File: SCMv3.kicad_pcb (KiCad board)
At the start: 2 copper layers, 58.7 x 110.9 mm, 122 parts, among them IC1 40106, IC2 40106, IC3 TL082, J1 ISP, J1-OUT8 JACK-MONO-SWB, J2 Conn_01x02, J2-OUT7 JACK-MONO-SWB, J3 POWER, J3-OUT6 JACK-MONO-SWB, J4-OUT5 JACK-MONO-SWB, J5-OUT4 JACK-MONO-SWB, J6-OUT3 JACK-MONO-SWB, J7-OUT2 JACK-MONO-SWB, J8-OUT1 JACK-MONO-SWB, J9-CLK_IN1 JCLK_IN, Q1 Si2318, Q2 Si2318, Q3 Si2318, Q4 Si2318, U1 ATmega328-A, Y1 16MHz_18pF_FA238

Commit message: Moved XTAL caps (C4, C5) GND trace to go directly to uc (U1)
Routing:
- net GND: track 698.8 -> 691.5 mm, vias 56 -> 54
- net +5V: track 225.1 -> 224.6 mm
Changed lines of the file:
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@@
     (effects (font (size 0.9652 0.9652) (thickness 0.12192)) (justify left bottom mirror))
   )
-  (segment (start 19.55 77.67) (end 19.55 79.45) (width 0.2032) (layer "F.Cu") (net 1))
   (segment (start 19.38 69.08) (end 19.68 68.78) (width 0.25) (layer "F.Cu") (net 1))
   (segment (start 6.98 85.52) (end 9.3 83.2) (width 0.25) (layer "F.Cu") (net 1))
@@
   (segment (start 31.82 104.3325) (end 31.14 103.6525) (width 0.2032) (layer "F.Cu") (net 1))
   (segment (start 31.09 79.3282) (end 30.9282 79.49) (width 0.2032) (layer "F.Cu") (net 1))
+  (segment (start 16.908889 73.061111) (end 17.94 72.03) (width 0.2032) (layer "F.Cu") (net 1))
   (segment (start 6.280902 85.52) (end 6.98 85.52) (width 0.25) (layer "F.Cu") (net 1))
   (segment (start 19.59 71.904022) (end 19.59 70.98) (width 0.25) (layer "F.Cu") (net 1))
@@
   (segment (start 34.03 52.99) (end 37.01 55.97) (width 0.2032) (layer "F.Cu") (net 1))
   (segment (start 13.67 88.43076) (end 11.11076 88.43076) (width 0.25) (layer "F.Cu") (net 1))
-  (segment (start 19.55 79.45) (end 20.04 79.94) (width 0.2032) (layer "F.Cu") (net 1))
   (segment (start 21.19 79.02) (end 21.19 80.57) (width 0.25) (layer "F.Cu") (net 1))
   (segment (start 55.84 62.1) (end 57.0738 63.3338) (width 0.2032) (layer "F.Cu") (net 1))
@@
   (segment (start 8.67 33.42) (end 8.67 31.69) (width 0.2032) (layer "F.Cu") (net 1))
   (segment (start 34.03 52.18) (end 34.03 52.99) (width 0.2032) (layer "F.Cu") (net 1))
+  (segment (start 16.908889 74.588889) (end 16.908889 73.061111) (width 0.2032) (layer "F.Cu") (net 1))
   (segment (start 4.83 86.57076) (end 5.230142 86.57076) (width 0.25) (layer "F.Cu") (net 1))
+  (segment (start 17.94 72.03) (end 17.99 72.03) (width 0.2032) (layer "F.Cu") (net 1))
   (segment (start 22.1 94.67) (end 22.1 95.90924) (width 0.2032) (layer "F.Cu") (net 1))
   (segment (start 14.330143 79.639857) (end 15.07 78.9) (width 0.25) (layer "F.Cu") (net 1))
@@
   (segment (start 13.823801 15.056199) (end 13.95 14.93) (width 0.25) (layer "F.Cu") (net 1))
   (segment (start 21.13 47.33) (end 18.87 47.33) (width 0.25) (layer "F.Cu") (net 1))
+  (segment (start 17.71 75.39) (end 16.908889 74.588889) (width 0.2032) (layer "F.Cu") (net 1))
   (segment (start 21.19 80.57) (end 21.95 81.33) (width 0.25) (layer "F.Cu") (net 1))
   (segment (start 33.8632 51.31) (end 31.82 51.31) (width 0.2032) (layer "F.Cu") (net 1))
@@
   (via (at 27.14 62.78) (size 0.8) (drill 0.4) (layers "F.Cu" "B.Cu") (net 1))
   (via (at 31.38 50.87) (size 0.8) (drill 0.4) (layers "F.Cu" "B.Cu") (net 1))
-  (via (at 20.04 79.94) (size 0.8) (drill 0.4) (layers "F.Cu" "B.Cu") (net 1))
   (via (at 27.14 62.78) (size 0.8) (drill 0.4) (layers "F.Cu" "B.Cu") (net 1))
   (via (at 21.95 81.33) (size 0.8) (drill 0.4) (layers "F.Cu" "B.Cu") (net 1))
   (via (at 13.099299 72.56) (size 0.8) (drill 0.4) (layers "F.Cu" "B.Cu") (net 1))
-  (via (at 20.04 79.94) (size 0.8) (drill 0.4) (layers "F.Cu" "B.Cu") (net 1))
   (via (at 24.39 17.6) (size 0.8) (drill 0.4) (layers "F.Cu" "B.Cu") (net 1))
   (via (at 37.01 55.97) (size 0.8) (drill 0.4) (layers "F.Cu" "B.Cu") (net 1))
@@
   (via (at 55.84 62.1) (size 0.8) (drill 0.4) (layers "F.Cu" "B.Cu") (net 1))
   (via (at 19.68 68.78) (size 0.8) (drill 0.4) (layers "F.Cu" "B.Cu") (net 1))
-  (segment (start 18.81 81.17) (end 13.722306 81.17) (width 0.2032) (layer "B.Cu") (net 1))
   (segment (start 22.6403 9.0297) (end 25.527 9.0297) (width 0.2032) (layer "B.Cu") (net 1))
   (segment (start 10.337963 72.629457) (end 13.029844 72.629457) (width 0.2032) (layer "B.Cu") (net 1))
@@
   (segment (start 27.14 67.5) (end 25.527 69.113) (width 0.2032) (layer "B.Cu") (net 1))
   (segment (start 6.623857 44.333857) (end 12.192163 44.333857) (width 0.25) (layer "B.Cu") (net 1))
-  (segment (start 13.722306 81.17) (end 12.192163 79.639857) (width 0.2032) (layer "B.Cu") (net 1))
   (segment (start 5.24 88.43) (end 4.75 87.94) (width 0.25) (layer "B.Cu") (net 1))
   (segment (start 22.57 9.1) (end 22.6403 9.0297) (width 0.2032) (layer "B.Cu") (net 1))
@@
   (segment (start 27.94 85.2297) (end 25.527 85.2297) (width 0.25) (layer "B.Cu") (net 1))
   (segment (start 19.12 27.07) (end 18.03 25.98) (width 0.2032) (layer "B.Cu") (net 1))
-  (segment (start 20.04 79.94) (end 18.81 81.17) (width 0.2032) (layer "B.Cu") (net 1))
   (segment (start 26.59 104.64) (end 25.91 105.32) (width 0.2032) (layer "B.Cu") (net 1))
   (segment (start 25.527 26.673) (end 25.527 21.7297) (width 0.2032) (layer "B.Cu") (net 1))
@@
   (segment (start 6.159663 38.225157) (end 6.159663 42.623765) (width 0.2032) (layer "F.Cu") (net 2))
   (segment (start 8.82 46.85) (end 8.84 46.87) (width 0.2032) (layer "F.Cu") (net 2))
-  (segment (start 21.1 59.26) (end 21.1 59.81) (width 0.2032) (layer "F.Cu") (net 2))
   (segment (start 7.38924 86.57076) (end 8.6 85.36) (width 0.2032) (layer "F.Cu") (net 2))
   (segment (start 5.257963 54.976457) (end 5.257963 60.371973) (width 0.2032) (layer "F.Cu") (net 2))
@@
   (segment (start 28.725899 54.155899) (end 24.42 49.85) (width 0.2032) (layer "B.Cu") (net 43))
   (segment (start 21.76 16.05) (end 21.73 16.08) (width 0.2032) (layer "F.Cu") (net 44))
+  (segment (start 34.165 4.995) (end 32.447289 6.712711) (width 0.2032) (layer "F.Cu") (net 44))
   (segment (start 21.73 16.08) (end 21.73 20.33) (width 0.2032) (layer "F.Cu") (net 44))
+  (segment (start 35.51 4.995) (end 34.165 4.995) (width 0.2032) (layer "F.Cu") (net 44))
   (segment (start 21.73 22.24898) (end 20.03898 23.94) (width 0.2032) (layer "F.Cu") (net 44))
-  (segment (start 34.807778 4.995) (end 28.89 10.912778) (width 0.2032) (layer "F.Cu") (net 44))
-  (segment (start 28.89 10.912778) (end 28.89 12.42) (width 0.2032) (layer "F.Cu") (net 44))
+  (segment (start 32.447289 8.862711) (end 28.89 12.42) (width 0.2032) (layer "F.Cu") (net 44))
   (segment (start 21.73 20.33) (end 21.73 22.24898) (width 0.2032) (layer "F.Cu") (net 44))
-  (segment (start 35.51 4.995) (end 34.807778 4.995) (width 0.2032) (layer "F.Cu") (net 44))
+  (segment (start 32.447289 6.712711) (end 32.447289 8.862711) (width 0.2032) (layer "F.Cu") (net 44))
   (via (at 21.76 16.05) (size 0.8) (drill 0.4) (layers "F.Cu" "B.Cu") (net 44))
   (via (at 21.76 16.05) (size 0.8) (drill 0.4) (layers "F.Cu" "B.Cu") (net 44))
@@
   (segment (start 40.461289 82.234111) (end 40.461289 92.914389) (width 0.2032) (layer "B.Cu") (net 62))
   (segment (start 41.3124 7.088) (end 40.461289 7.939111) (width 0.2032) (layer "B.Cu") (net 62))
-  (segment (start 35.28611 5.86889) (end 34.583889 5.86889) (width 0.2032) (layer "F.Cu") (net 63))
-  (segment (start 34.583889 10.306111) (end 32.75 12.14) (width 0.2032) (layer "F.Cu") (net 63))
-  (segment (start 34.583889 5.86889) (end 34.583889 10.306111) (width 0.2032) (layer "F.Cu") (net 63))
-  (segment (start 35.51 5.645) (end 35.28611 5.86889) (width 0.2032) (layer "F.Cu") (net 63))
+  (segment (start 35.51 5.645) (end 34.565 5.645) (width 0.2032) (layer "F.Cu") (net 63))
+  (segment (start 34.12 10.77) (end 32.75 12.14) (width 0.2032) (layer "F.Cu") (net 63))
+  (segment (start 34.12 6.09) (end 34.12 10.77) (width 0.2032) (layer "F.Cu") (net 63))
+  (segment (start 34.565 5.645) (end 34.12 6.09) (width 0.2032) (layer "F.Cu") (net 63))
   (segment (start 27.24 2.74) (end 27.56 2.42) (width 0.2032) (layer "F.Cu") (net 64))
   (segment (start 27.56 4.58) (end 27.24 4.9) (width 0.25) (layer "F.Cu") (net 64))
@@
   (segment (start 27.24 4.9) (end 27.24 2.74) (width 0.2032) (layer "F.Cu") (net 64))
   (segment (start 29.61 4.995) (end 27.335 4.995) (width 0.2032) (layer "F.Cu") (net 64))
-  (segment (start 33.36548 5.645) (end 37.62048 1.39) (width 0.2032) (layer "F.Cu") (net 65))
-  (segment (start 37.62048 1.39) (end 50.4628 1.39) (width 0.2032) (layer "F.Cu") (net 65))
-  (segment (start 50.4628 1.39) (end 54.6608 5.588) (width 0.2032) (layer "F.Cu") (net 65))
-  (segment (start 29.61 5.645) (end 33.36548 5.645) (width 0.2032) (layer "F.Cu") (net 65))
+  (segment (start 29.61 5.645) (end 31.934852 5.645) (width 0.2032) (layer "F.Cu") (net 65))
+  (segment (start 50.1328 1.06) (end 54.6608 5.588) (width 0.2032) (layer "F.Cu") (net 65))
+  (segment (start 36.519852 1.06) (end 50.1328 1.06) (width 0.2032) (layer "F.Cu") (net 65))
+  (segment (start 31.934852 5.645) (end 36.519852 1.06) (width 0.2032) (layer "F.Cu") (net 65))
   (segment (start 29.61 5.645) (end 29.61 6.295) (width 0.2032) (layer "F.Cu") (net 65))
   (segment (start 24.83 2.23) (end 25.02 2.42) (width 0.2032) (layer "F.Cu") (net 66))

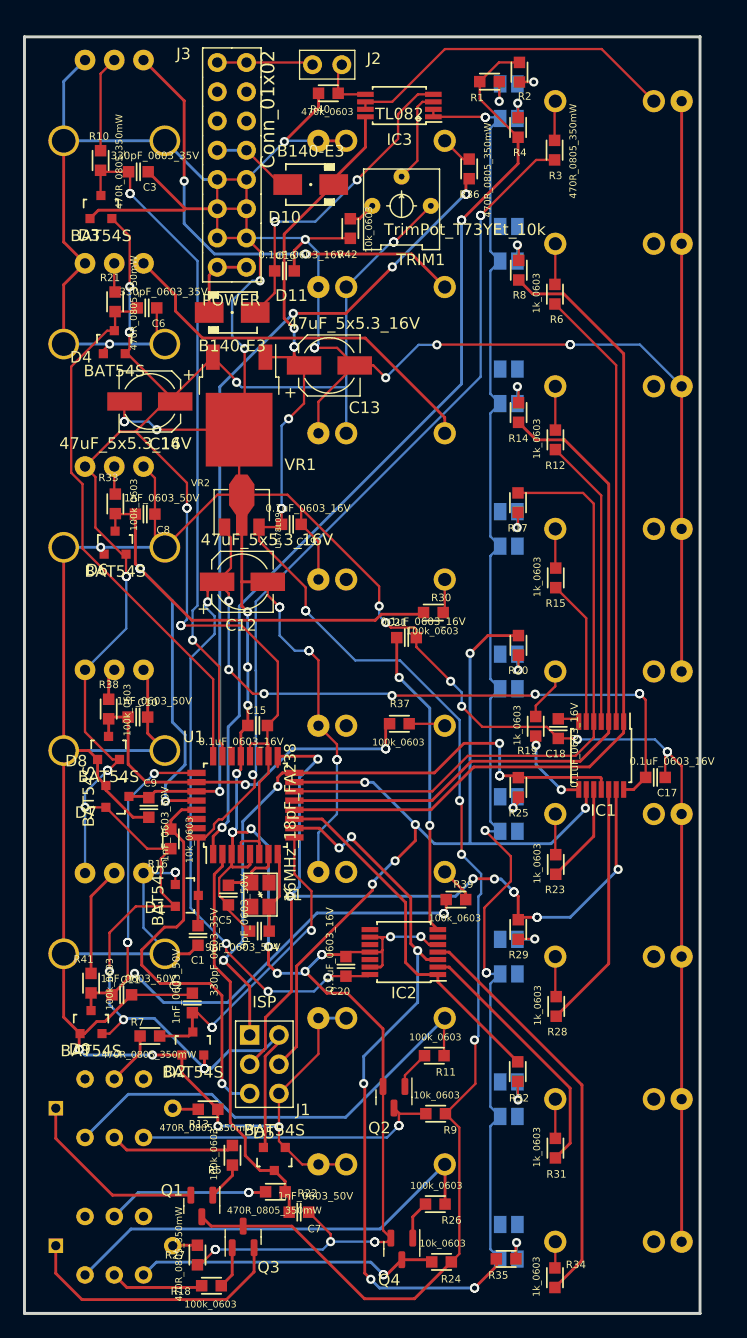
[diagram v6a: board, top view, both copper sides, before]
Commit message: Removed all duplicate Vias. Project ignores silk overlap DRC errors
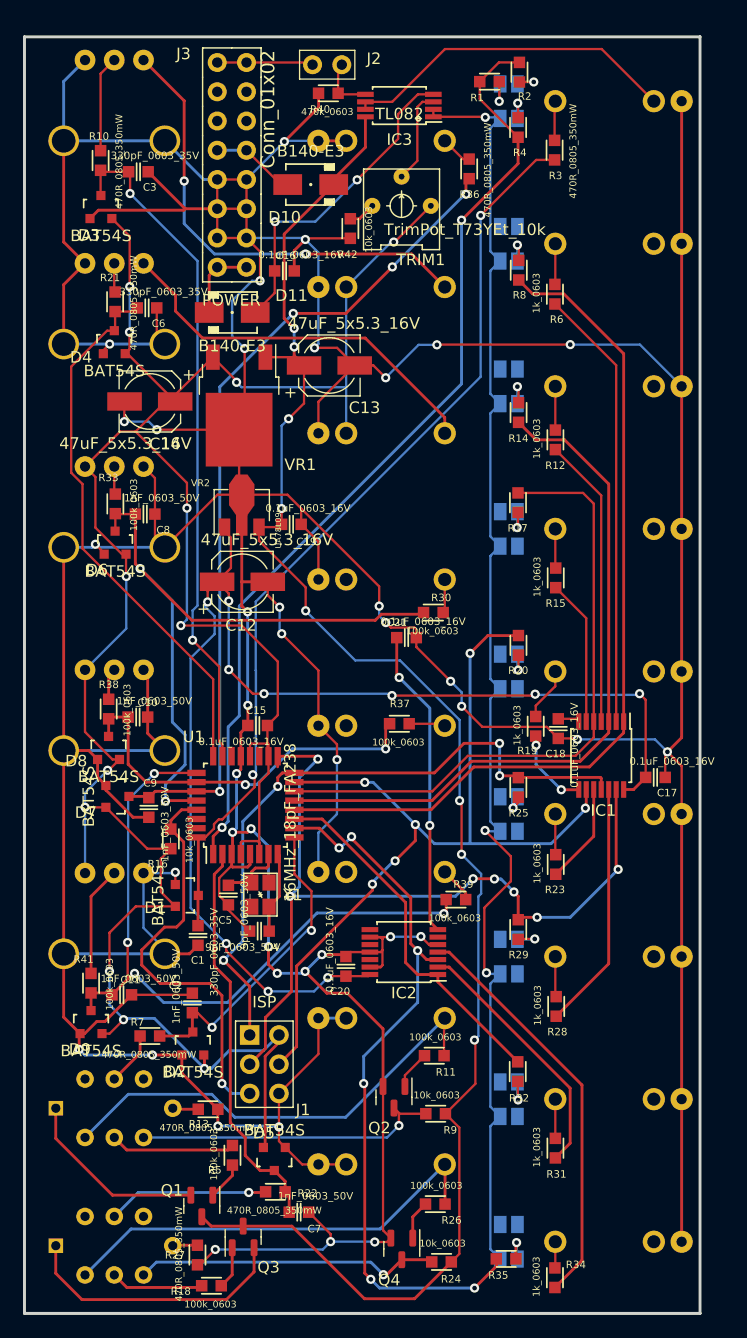
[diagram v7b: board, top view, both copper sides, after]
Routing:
- net GND: track 691.5 -> 699.0 mm, vias 54 -> 40
- net Net-(BMUTE1-Pad6): vias 2 -> 1
- net Net-(BMUTE1-Pad2): vias 2 -> 1
- net Net-(BFAST1-Pad6): vias 2 -> 1
- net /VREF: vias 5 -> 3
- net /UC_SYNC: vias 5 -> 4
- net /UC_SKIP: vias 3 -> 2
- net /UC_SHUFFLE: vias 3 -> 2
- net /UC_ROTATE: vias 3 -> 2
- net /UC_PW: vias 7 -> 4
- net /UC_OUT8: vias 7 -> 6
- net /UC_OUT6_SCK: vias 9 -> 7
- net /UC_OUT5_MISO: vias 5 -> 4
- net /UC_LED_IN: vias 3 -> 2
- net /UC_FAST: vias 3 -> 2
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
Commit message: SILK
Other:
- board text added: "-12V"
- board text added: "ISP"
- board text added: "POWER"
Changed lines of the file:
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@@
     (property "Specifications" "Vreg 5.0V, Iout>500mA, Vin>7V")
     (attr smd)
-    (fp_text reference "VR1" (at 5.14 -5.31 180) (layer "F.SilkS")
+    (fp_text reference "VR1" (at 5.06 -4.95 180) (layer "F.SilkS")
       (effects (font (size 1 1) (thickness 0.15)))
     )
@@
       (effects (font (size 1 1) (thickness 0.15)) (justify left bottom))
     )
-    (fp_text value "POWER" (at -0.05 11.75) (layer "F.SilkS")
+    (fp_text value "POWER" (at -3.28 5.09 90) (layer "F.SilkS")
       (effects (font (size 1 1) (thickness 0.15)))
     )
@@
     (property "Specifications" "470R, 1%, 1/10W, 0603")
     (attr smd)
-    (fp_text reference "R21" (at -2.09 0.44 180) (layer "F.SilkS")
+    (fp_text reference "R21" (at -0.78 1.75 180) (layer "F.SilkS")
       (effects (font (size 0.65 0.65) (thickness 0.15)))
     )
@@
     (property "Specifications" "Dual schottky diode BAT54S")
     (attr smd)
-    (fp_text reference "D4" (at -2.89 1.31) (layer "F.SilkS")
+    (fp_text reference "D4" (at -0.77 2.36) (layer "F.SilkS")
       (effects (font (size 1 1) (thickness 0.15)))
     )
@@
     (property "Specifications" "MOSFET N-chan, 40Vds, Vgs_th=1.2V, Rds=42mOhms")
     (attr smd)
-    (fp_text reference "Q2" (at 2.66 1.27 180) (layer "F.SilkS")
+    (fp_text reference "Q2" (at -0.5 2.81 180) (layer "F.SilkS")
       (effects (font (size 1 1) (thickness 0.15)))
     )
@@
     (property "Specifications" "330pF, Min 35V, C0G/NP0, 5%")
     (attr smd)
-    (fp_text reference "C6" (at 1 1.36) (layer "F.SilkS")
+    (fp_text reference "C6" (at 1.17 -1.18) (layer "F.SilkS")
       (effects (font (size 0.65 0.65) (thickness 0.15)))
     )
@@
     (property "Specifications" "100K, 1%, 1/10W, 0603")
     (attr smd)
-    (fp_text reference "R41" (at -2.07 0.65 180) (layer "F.SilkS")
+    (fp_text reference "R41" (at -2.08 -0.34 180) (layer "F.SilkS")
       (effects (font (size 0.65 0.65) (thickness 0.15)))
     )
@@
     (property "Specifications" "10K, 1%, 1/10W, 0603")
     (attr smd)
-    (fp_text reference "R16" (at 2.17 1.14 180) (layer "F.SilkS")
+    (fp_text reference "R16" (at 2.19 -0.83 180) (layer "F.SilkS")
       (effects (font (size 0.65 0.65) (thickness 0.15)))
     )
@@
     (fp_line (start -2.71 -4.05) (end 2.71 -4.05) (layer "F.CrtYd") (width 0.05))
     (pad "1" thru_hole rect locked (at -1.27 -2.54 180) (size 1.7 1.7) (drill 1) (layers *.Cu *.Mask)
-      (net 60 "/UC_OUT5_MISO") (pinfunction "+12V") (pintype "passive"))
+      (net 60 "/UC_OUT5_MISO") (pinfunction "+12V"))
     (pad "2" thru_hole oval locked (at 1.27 -2.54 180) (size 1.7 1.7) (drill 1) (layers *.Cu *.Mask)
-      (net 2 "+5V") (pinfunction "+12V") (pintype "passive"))
+      (net 2 "+5V") (pinfunction "+12V"))
     (pad "3" thru_hole oval locked (at -1.27 0 180) (size 1.7 1.7) (drill 1) (layers *.Cu *.Mask)
-      (net 61 "/UC_OUT6_SCK") (pinfunction "GND") (pintype "passive"))
+      (net 61 "/UC_OUT6_SCK") (pinfunction "GND"))
     (pad "4" thru_hole oval locked (at 1.27 0 180) (size 1.7 1.7) (drill 1) (layers *.Cu *.Mask)
-      (net 54 "/UC_OUT4_MOSI") (pinfunction "GND") (pintype "passive"))
+      (net 54 "/UC_OUT4_MOSI") (pinfunction "GND"))
     (pad "5" thru_hole oval locked (at -1.27 2.54 180) (size 1.7 1.7) (drill 1) (layers *.Cu *.Mask)
-      (net 121 "/RESET") (pinfunction "GND") (pintype "passive"))
+      (net 121 "/RESET") (pinfunction "GND"))
     (pad "6" thru_hole oval locked (at 1.27 2.54 180) (size 1.7 1.7) (drill 1) (layers *.Cu *.Mask)
-      (net 1 "GND") (pinfunction "GND") (pintype "passive"))
+      (net 1 "GND") (pinfunction "GND"))
     (model "${KISYS3DMOD}/Connector_PinHeader_2.54mm.3dshapes/PinHeader_2x03_P2.54mm_Vertical.step"
       (offset (xyz -1.27 2.54 0))
@@
     (property "Specifications" "100K, 1%, 1/10W, 0603")
     (attr smd)
-    (fp_text reference "R38" (at -2.12 -0.01 180) (layer "F.SilkS")
+    (fp_text reference "R38" (at -1.18 1.89 180) (layer "F.SilkS")
       (effects (font (size 0.65 0.65) (thickness 0.15)))
     )
@@
     (property "Specifications" "100K, 1%, 1/10W, 0603")
     (attr smd)
-    (fp_text reference "R33" (at -2.27 0.6 180) (layer "F.SilkS")
+    (fp_text reference "R33" (at -1.18 1.77 180) (layer "F.SilkS")
       (effects (font (size 0.65 0.65) (thickness 0.15)))
     )
@@
     (property "Specifications" "SCHOTTKY Diode SMA Vrrm>=40V If>=1.0A, Ifsm>=1.5A")
     (attr smd)
-    (fp_text reference "D10" (at 2.27 -2.84) (layer "F.SilkS")
+    (fp_text reference "D10" (at 0.85 -2.8) (layer "F.SilkS")
       (effects (font (size 1.016 1.016) (thickness 0.1524)))
     )
@@
     (property "Specifications" "470R, 1%, 1/10W, 0603")
     (attr smd)
-    (fp_text reference "R27" (at -0.01 -1.95 180) (layer "F.SilkS")
+    (fp_text reference "R27" (at -1.29 -1.81 180) (layer "F.SilkS")
       (effects (font (size 0.65 0.65) (thickness 0.15)))
     )
@@
     (property "Specifications" "1nF, 50V, 10%, C0G (NP0) or similar")
     (attr smd)
-    (fp_text reference "C8" (at 1.57 1.38) (layer "F.SilkS")
+    (fp_text reference "C8" (at 1.15 -1.27) (layer "F.SilkS")
       (effects (font (size 0.65 0.65) (thickness 0.15)))
     )
@@
     (property "Specifications" "Dual schottky diode BAT54S")
     (attr smd)
-    (fp_text reference "D7" (at 1.4 2.74 180) (layer "F.SilkS")
+    (fp_text reference "D7" (at -0.02 2.83 180) (layer "F.SilkS")
       (effects (font (size 1 1) (thickness 0.15)))
     )
@@
     (property "Specifications" "100K, 1%, 1/10W, 0603")
     (attr smd)
-    (fp_text reference "R39" (at -0.65 1.33) (layer "F.SilkS")
+    (fp_text reference "R39" (at -1.46 1.37) (layer "F.SilkS")
       (effects (font (size 0.65 0.65) (thickness 0.15)))
     )
@@
     (property "Specifications" "8-bit Microcontrollers - MCU AVR 32K FLSH, 1K EE 2K SRAM - 20 MHz")
     (attr smd)
-    (fp_text reference "U1" (at 5.94 -4.5 180) (layer "F.SilkS")
+    (fp_text reference "U1" (at 6.32 -3.06 180) (layer "F.SilkS")
       (effects (font (size 1 1) (thickness 0.15)))
     )
@@
     (property "Specifications" "100K, 1%, 1/10W, 0603")
     (attr smd)
-    (fp_text reference "R30" (at -0.68 1.29) (layer "F.SilkS")
+    (fp_text reference "R30" (at 1.15 1.34) (layer "F.SilkS")
       (effects (font (size 0.65 0.65) (thickness 0.15)))
     )
@@
     (property "Specifications" "0.1uF, Min. 16V 10%, X7R or X5R or similar")
     (attr smd)
-    (fp_text reference "C19" (at 1.3 1.51) (layer "F.SilkS")
+    (fp_text reference "C19" (at 0.62 -1.6) (layer "F.SilkS")
       (effects (font (size 0.65 0.65) (thickness 0.15)))
     )
@@
     (property "Specifications" "Dual schottky diode BAT54S")
     (attr smd)
-    (fp_text reference "D8" (at -2.81 1.14) (layer "F.SilkS")
+    (fp_text reference "D8" (at -1.92 -1.84) (layer "F.SilkS")
       (effects (font (size 1 1) (thickness 0.15)))
     )
@@
   (gr_line (start 0 0) (end 58.674 0) (layer "Edge.Cuts") (width 0.254))
   (gr_line (start 0 110.871) (end 0 0) (layer "Edge.Cuts") (width 0.254))
+  (gr_text "-12V" (at 13.55 20.25) (layer "F.SilkS")
+    (effects (font (size 0.762 0.762) (thickness 0.15)))
+  )
+  (gr_text "ISP" (at 20.85 84.67) (layer "F.SilkS")
+    (effects (font (size 1 1) (thickness 0.15)))
+  )
+  (gr_text "POWER" (at 14.26 13.35 90) (layer "F.SilkS")
+    (effects (font (size 1 1) (thickness 0.15)))
+  )
   (gr_text "\n" (at 39.8956 5.967 90) (layer "Dwgs.User")
     (effects (font (size 0.9652 0.9652) (thickness 0.12192)) (justify left bottom mirror))
